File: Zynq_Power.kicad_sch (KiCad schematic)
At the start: 51 parts, among them U200 XC7Z010-2CLG400I

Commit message: Finished page 3 of schematic: Zynq Config, JTAG, Debug
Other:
- title: ZeBra-X: A Xilinx Zynq Demo Board -> Zynq Power
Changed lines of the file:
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@@
   (paper "A3")
   (title_block
-    (title "ZeBra-X: A Xilinx Zynq Demo Board")
+    (title "Zynq Power")
     (date "2023-12-09")
     (rev "-")
@@
       (effects (font (size 1.27 1.27)) hide)
     )
+    (pin "F6")
+    (pin "F9")
+    (pin "G6")
+    (pin "J6")
+    (pin "K10")
+    (pin "K9")
+    (pin "L10")
+    (pin "L6")
+    (pin "L9")
+    (pin "M10")
+    (pin "M6")
+    (pin "M9")
+    (pin "R10")
+    (pin "R11")
     (pin "C19")
     (pin "F18")
@@
       (effects (font (size 1.27 1.27)) hide)
     )
+    (pin "F6")
+    (pin "F9")
+    (pin "G6")
+    (pin "J6")
+    (pin "K10")
+    (pin "K9")
+    (pin "L10")
+    (pin "L6")
+    (pin "L9")
+    (pin "M10")
+    (pin "M6")
+    (pin "M9")
+    (pin "R10")
+    (pin "R11")
     (pin "C19")
     (pin "F18")
@@
       (effects (font (size 1.27 1.27)) hide)
     )
+    (pin "F6")
+    (pin "F9")
+    (pin "G6")
+    (pin "J6")
+    (pin "K10")
+    (pin "K9")
+    (pin "L10")
+    (pin "L6")
+    (pin "L9")
+    (pin "M10")
+    (pin "M6")
+    (pin "M9")
+    (pin "R10")
+    (pin "R11")
     (pin "C19")
     (pin "F18")
@@
       (effects (font (size 1.27 1.27)) hide)
     )
+    (pin "F6")
+    (pin "F9")
+    (pin "G6")
+    (pin "J6")
+    (pin "K10")
+    (pin "K9")
+    (pin "L10")
+    (pin "L6")
+    (pin "L9")
+    (pin "M10")
+    (pin "M6")
+    (pin "M9")
+    (pin "R10")
+    (pin "R11")
     (pin "C19")
     (pin "F18")

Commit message: Added page '[7] 1GB DDR3L Modules'
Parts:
- renumbered C103 to C200, C129 to C201, C129 to C202, C129 to C203, C103 to C204, C129 to C205, C129 to C206, C129 to C207, C129 to C208, C103 to C209, C129 to C210, C129 to C211, C103 to C212, C129 to C213, C129 to C214, C129 to C215, C129 to C216, C129 to C217, C129 to C218, C129 to C219, C129 to C220, C103 to C221, C129 to C222, C129 to C223, C103 to C224, C129 to C225, C129 to C226, C129 to C227, C129 to C228, C129 to C229, C103 to C230, C129 to C231, C129 to C232, C103 to C233, C103 to C234, C103 to C235, C129 to C236, C129 to C237, C129 to C238, C129 to C239, C129 to C240, C129 to C241, C129 to C242, C129 to C243, C129 to C244, C129 to C245, C129 to C246, C129 to C247, C103 to C248

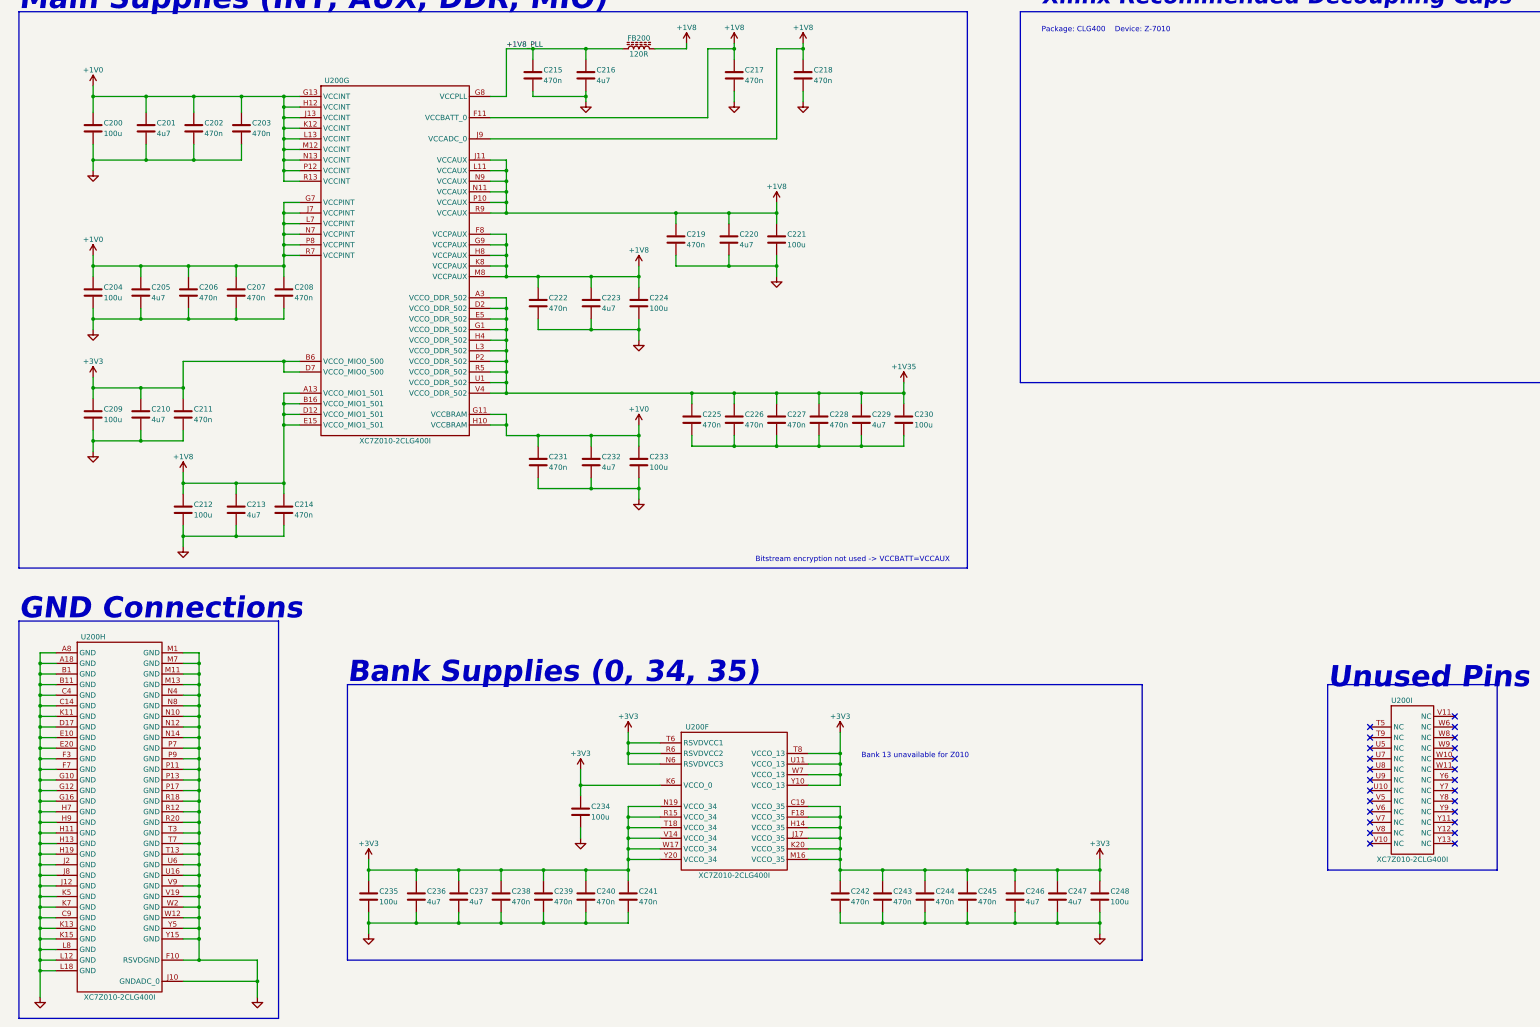
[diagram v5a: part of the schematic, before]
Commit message: Finished first pass of schematic, needs netclass assignments and double check
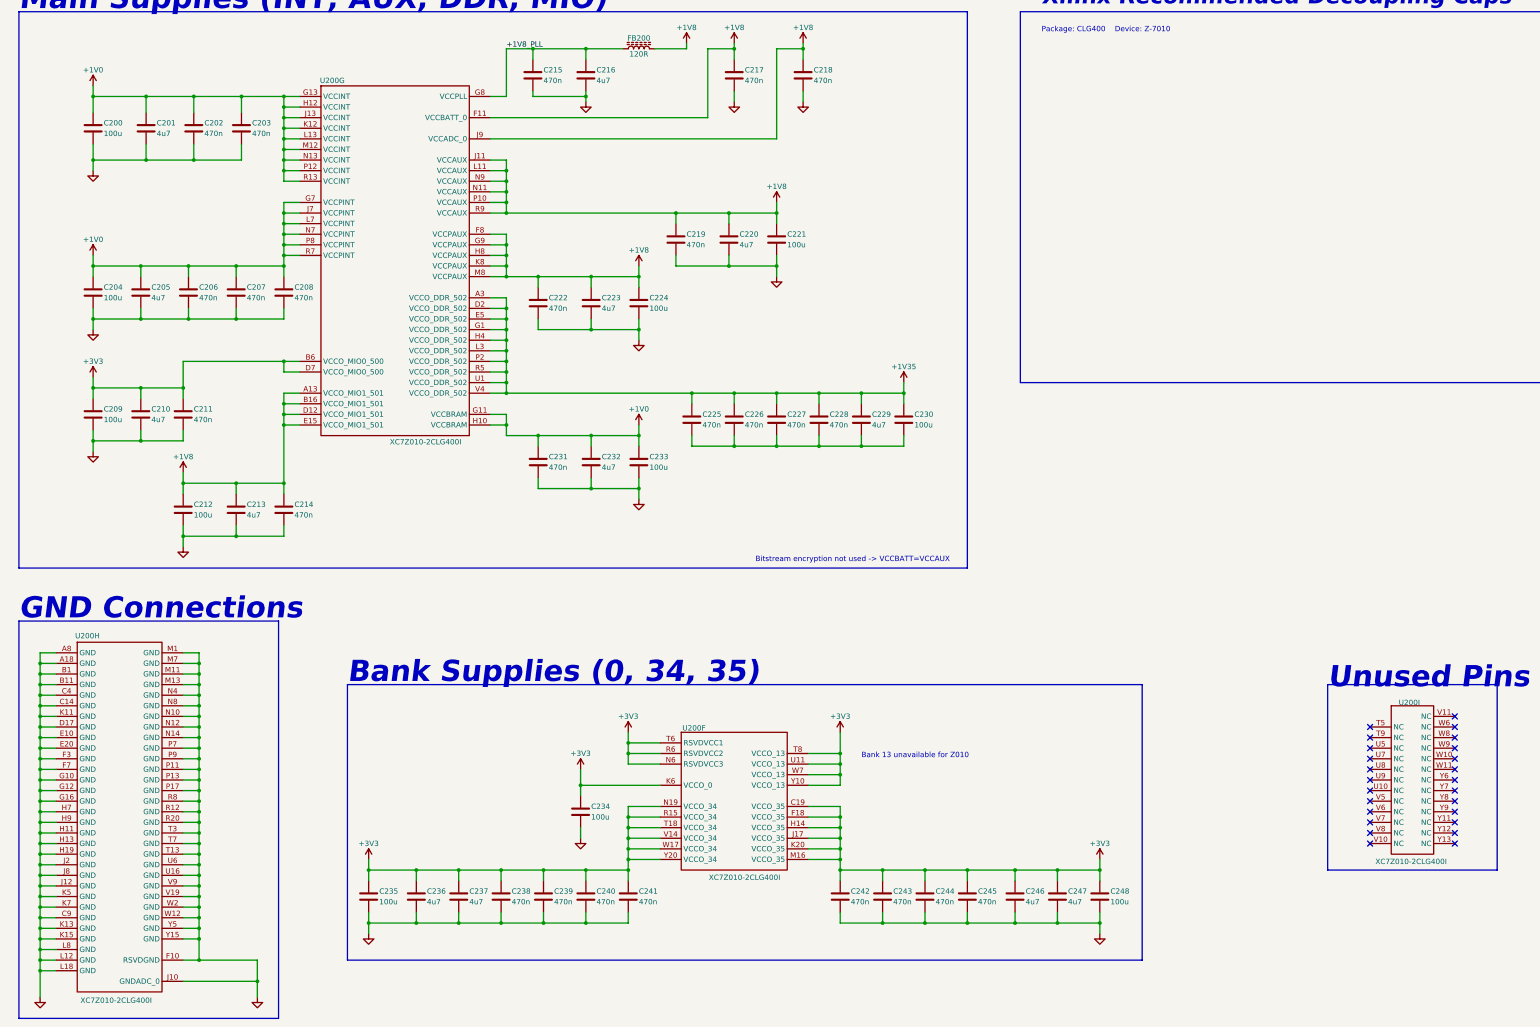
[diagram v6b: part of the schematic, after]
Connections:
- net GND: now also U200.R8 (GND); no longer U200.R18 (GND)
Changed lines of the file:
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@@
 		(dnp no)
 		(property "Reference" "U200"
-			(at 35.56 190.5 0)
+			(at 31.242 190.246 0)
 			(effects
 				(font
 					(size 1.27 1.27)
 				)
+				(justify left)
 			)
 		)
 		(property "Value" "XC7Z010-2CLG400I"
-			(at 41.91 276.86 0)
+			(at 32.512 277.622 0)
 			(effects
 				(font
 					(size 1.27 1.27)
 				)
+				(justify left)
 			)
 		)
@@
 		(pin "R17"
 		)
-		(pin "R18"
+		(pin "R8"
 		)
 		(pin "R19"
@@
 		)
 		(instances
-			(project "ZeBra-X"
+			(project ""
+				(path "/ec71d28a-654e-4dfb-b412-dd09b7b3e4b8/369d50d7-e508-4bcb-a2d0-a2c7d0c5b870"
+					(reference "U200")
+					(unit 8)
+				)
 				(path "/ec71d28a-654e-4dfb-b412-dd09b7b3e4b8/7bfac455-2207-4651-9024-5f4a3b59f883"
 					(reference "U200")
@@
 		(dnp no)
 		(property "Reference" "U200"
-			(at 93.98 57.15 0)
+			(at 89.916 57.15 0)
 			(effects
 				(font
 					(size 1.27 1.27)
 				)
+				(justify left)
 			)
 		)
 		(property "Value" "XC7Z010-2CLG400I"
-			(at 107.95 143.51 0)
+			(at 106.68 143.764 0)
 			(effects
 				(font
 					(size 1.27 1.27)
 				)
+				(justify left)
 			)
 		)
@@
 		(pin "R12"
 		)
-		(pin "R18"
+		(pin "R8"
 		)
 		(pin "R20"
@@
 		)
 		(instances
-			(project "ZeBra-X"
+			(project ""
+				(path "/ec71d28a-654e-4dfb-b412-dd09b7b3e4b8/369d50d7-e508-4bcb-a2d0-a2c7d0c5b870"
+					(reference "U200")
+					(unit 7)
+				)
 				(path "/ec71d28a-654e-4dfb-b412-dd09b7b3e4b8/7bfac455-2207-4651-9024-5f4a3b59f883"
 					(reference "U200")
@@
 	)
 	(symbol
+		(lib_name "XC7Z010-2CLG400I_3")
 		(lib_id "ZeBra-X:XC7Z010-2CLG400I")
 		(at 189.23 226.06 0)
@@
 		(dnp no)
 		(property "Reference" "U200"
-			(at 180.34 212.09 0)
+			(at 176.784 212.344 0)
 			(effects
 				(font
 					(size 1.27 1.27)
 				)
+				(justify left)
 			)
 		)
 		(property "Value" "XC7Z010-2CLG400I"
-			(at 189.23 247.65 0)
+			(at 183.134 248.158 0)
 			(effects
 				(font
 					(size 1.27 1.27)
 				)
+				(justify left)
 			)
 		)
@@
 		)
 		(instances
-			(project "ZeBra-X"
+			(project ""
+				(path "/ec71d28a-654e-4dfb-b412-dd09b7b3e4b8/369d50d7-e508-4bcb-a2d0-a2c7d0c5b870"
+					(reference "U200")
+					(unit 6)
+				)
 				(path "/ec71d28a-654e-4dfb-b412-dd09b7b3e4b8/7bfac455-2207-4651-9024-5f4a3b59f883"
 					(reference "U200")
@@
 	)
 	(symbol
+		(lib_name "XC7Z010-2CLG400I_2")
 		(lib_id "ZeBra-X:XC7Z010-2CLG400I")
 		(at 351.79 222.25 0)
@@
 		(dnp no)
 		(property "Reference" "U200"
-			(at 349.25 205.74 0)
+			(at 348.488 206.248 0)
 			(effects
 				(font
 					(size 1.27 1.27)
 				)
+				(justify left)
 			)
 		)
 		(property "Value" "XC7Z010-2CLG400I"
-			(at 351.79 243.84 0)
+			(at 342.9 244.348 0)
 			(effects
 				(font
 					(size 1.27 1.27)
 				)
+				(justify left)
 			)
 		)
@@
 		)
 		(instances
-			(project "ZeBra-X"
+			(project ""
+				(path "/ec71d28a-654e-4dfb-b412-dd09b7b3e4b8/369d50d7-e508-4bcb-a2d0-a2c7d0c5b870"
+					(reference "U200")
+					(unit 9)
+				)
 				(path "/ec71d28a-654e-4dfb-b412-dd09b7b3e4b8/7bfac455-2207-4651-9024-5f4a3b59f883"
 					(reference "U200")
